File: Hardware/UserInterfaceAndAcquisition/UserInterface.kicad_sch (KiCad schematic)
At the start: 50 parts, among them J2 Conn_02x06_Odd_Even, Q1 BC848, Q2 BC848, Q3 BC848, Q4 BC859, Q5 BC859, Q6 BC859, Q7 BC848, Q8 BC859, SW1 SW_Push, SW2 SW_Push

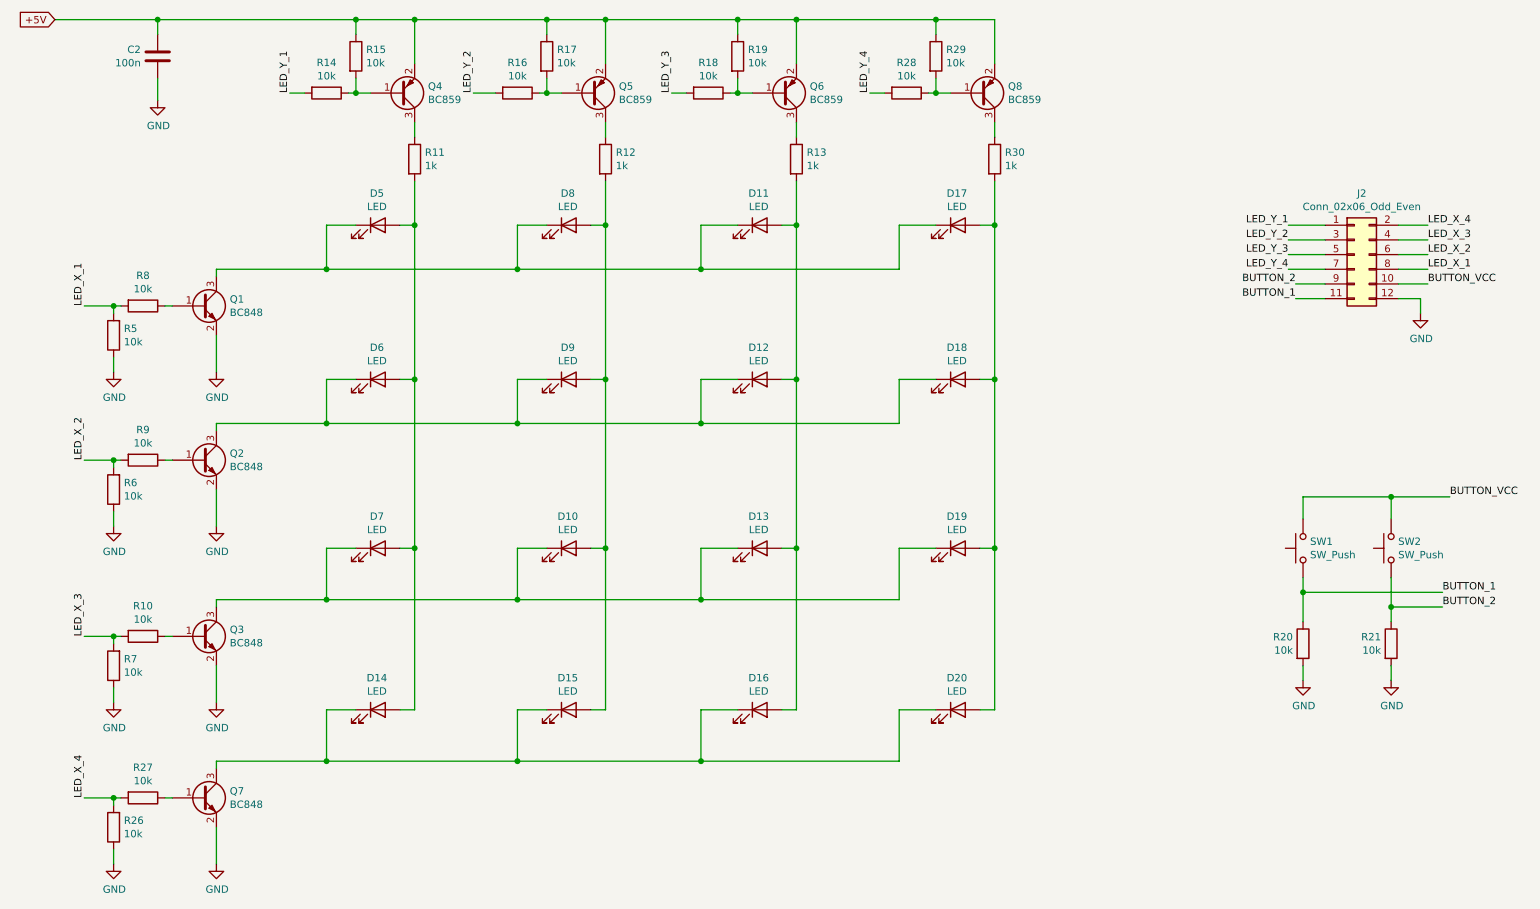
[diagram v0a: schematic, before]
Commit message: split PCB into separate designs
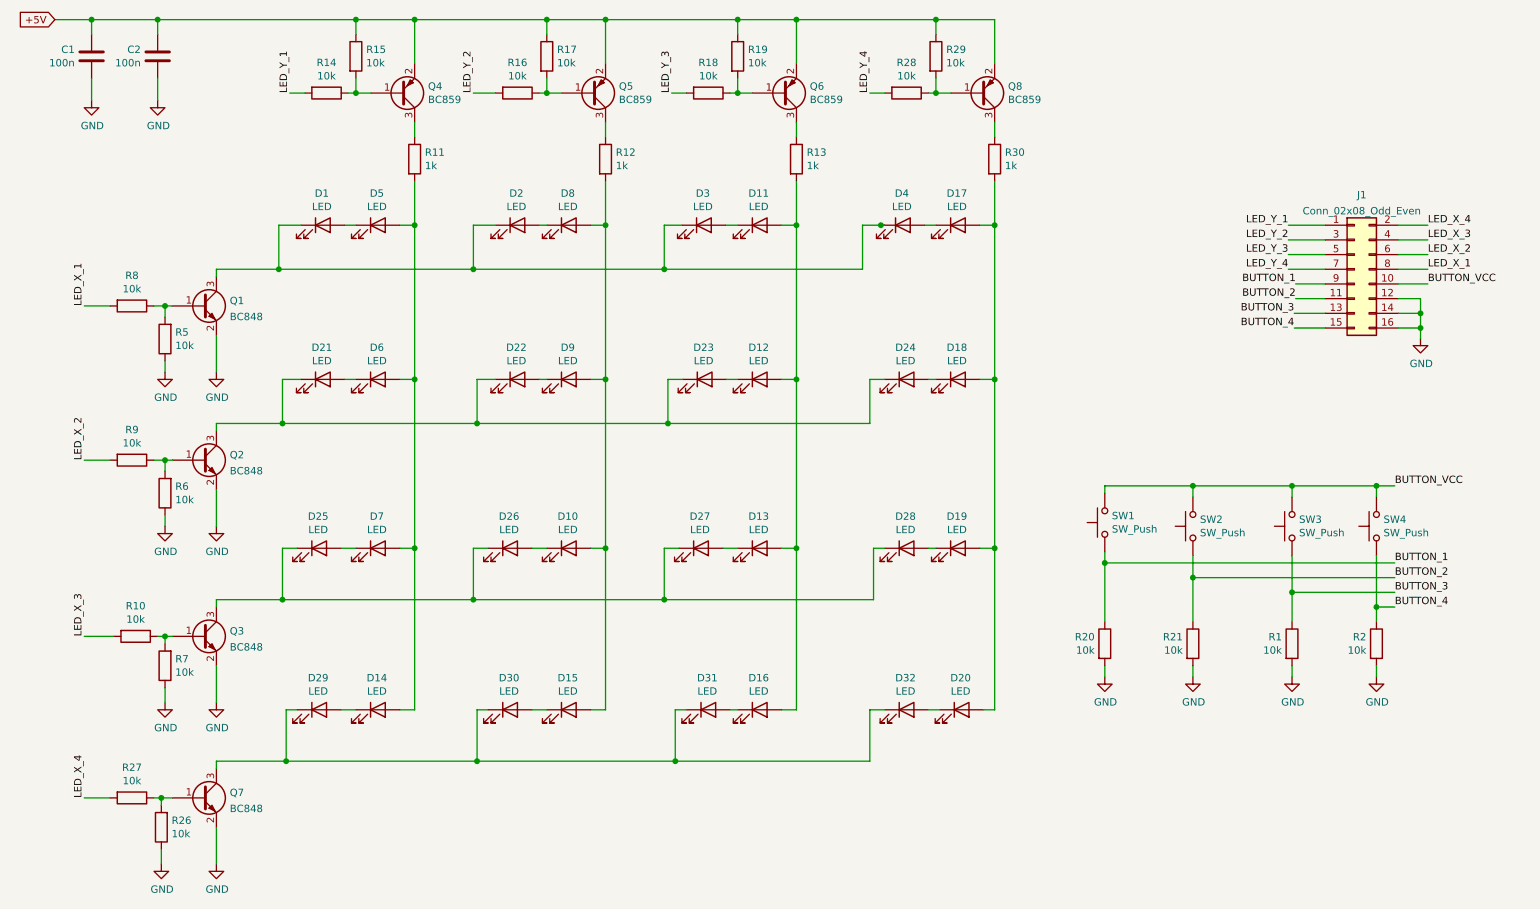
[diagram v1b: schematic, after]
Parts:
- removed J2: Conn_02x06_Odd_Even, Connector_PinHeader_2.54mm:PinHeader_2x06_P2.54mm_Horizontal, symbol Connector_Generic:Conn_02x06_Odd_Even
- added C1: 100n, Capacitor_SMD:C_0805_2012Metric, symbol Device:C
- added D1, D2, D21, D22, D23, D24, D25, D26, D27, D28, D29, D3, D30, D31, D32, D4: LED, LED_SMD:LED_0805_2012Metric, symbol Device:LED
- added J1: Conn_02x08_Odd_Even, Connector_PinHeader_2.54mm:PinHeader_2x08_P2.54mm_Horizontal, symbol Connector_Generic:Conn_02x08_Odd_Even
- added R1, R2: 10k, Resistor_SMD:R_0805_2012Metric, symbol Device:R
- added SW3, SW4: SW_Push, Button_Switch_THT:SW_PUSH_6mm, symbol Switch:SW_Push
- C2: footprint Capacitor_SMD:C_0805_2012Metric_Pad1.15x1.40mm_HandSolder -> Capacitor_SMD:C_0805_2012Metric
- D10, D11, D12, D13, D14, D15, D16, D17, D18, D19, D20, D5, D6, D7, D8, D9: footprint LED_THT:LED_D4.0mm -> LED_SMD:LED_0805_2012Metric
- R10, R14, R15, R16, R18, R19, R26, R27, R28, R29, R5, R6, R7, R8, R9: footprint Resistor_SMD:R_0402_1005Metric -> Resistor_SMD:R_0805_2012Metric
- R11, R12, R13, R20, R21, R30: footprint Resistor_SMD:R_0805_2012Metric_Pad1.15x1.40mm_HandSolder -> Resistor_SMD:R_0805_2012Metric
- SW1, SW2: footprint Button_Switch_SMD:SW_SPST_PTS645 -> Button_Switch_THT:SW_PUSH_6mm
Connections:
- net +5V: now also C1.1
- net BUTTON_1: now also J1.9 (Pin_9)
- net BUTTON_2: now also J1.11 (Pin_11)
- net BUTTON_VCC: now also J1.10 (Pin_10), SW3.2, SW4.2
- net GND: now also C1.2, J1.12 (Pin_12), J1.14 (Pin_14), J1.16 (Pin_16), R1.2, R2.2
- net LED_X_1: now also J1.8 (Pin_8); no longer R5.2
- net LED_X_2: now also J1.6 (Pin_6); no longer R6.2
- net LED_X_3: now also J1.4 (Pin_4); no longer R7.2
- net LED_X_4: now also J1.2 (Pin_2); no longer R26.2
- net LED_Y_1: now also J1.1 (Pin_1)
- net LED_Y_2: now also J1.3 (Pin_3)
- net LED_Y_3: now also J1.5 (Pin_5)
- net LED_Y_4: now also J1.7 (Pin_7)
- net at Q7.1 (B), R27.1: now also R26.2
- net at Q1.1 (B), R8.1: now also R5.2
- net at Q2.1 (B), R9.1: now also R6.2
- net at Q3.1 (B), R10.1: now also R7.2
- new net: D17.1 (K), D4.2 (A)
- new net: D18.1 (K), D24.2 (A)
- new net: D19.1 (K), D28.2 (A)
- new net: D14.1 (K), D29.2 (A)
- new net: D15.1 (K), D30.2 (A)
- new net: D16.1 (K), D31.2 (A)
- new net: D20.1 (K), D32.2 (A)
- new net: D1.2 (A), D5.1 (K)
- new net: D21.2 (A), D6.1 (K)
- new net: D25.2 (A), D7.1 (K)
- new net: D2.2 (A), D8.1 (K)
- new net: D22.2 (A), D9.1 (K)
- new net: D10.1 (K), D26.2 (A)
- new net: D11.1 (K), D3.2 (A)
- new net: D12.1 (K), D23.2 (A)
- new net: D13.1 (K), D27.2 (A)
- new net: D21.1 (K), D22.1 (K), D23.1 (K), D24.1 (K), Q2.3 (C)
- new net: D1.1 (K), D2.1 (K), D3.1 (K), D4.1 (K), Q1.3 (C)
- new net: D29.1 (K), D30.1 (K), D31.1 (K), D32.1 (K), Q7.3 (C)
- new net: D25.1 (K), D26.1 (K), D27.1 (K), D28.1 (K), Q3.3 (C)
- new net BUTTON_3: J1.13 (Pin_13), R1.1, SW3.1
- new net BUTTON_4: J1.15 (Pin_15), R2.1, SW4.1
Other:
- moved on the sheet: D20, R10, R20, R21, R26, R27, R5, R6, R7, R8, R9, SW1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
